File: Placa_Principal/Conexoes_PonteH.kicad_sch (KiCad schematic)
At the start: 6 parts, among them J2 Conn_01x02, J3 Conn_01x02, J4 Conn_01x02, J5 Conn_01x02, U4 L298N MODULE, U5 L298N MODULE

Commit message: Segundo commit
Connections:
- net at U4.2 (IN2L): no longer J3.1 (Pin_1)
- net at U4.1 (IN1L): no longer J3.2 (Pin_2)
- net at U5.1 (IN1L): no longer J5.2 (Pin_2)
- net at U5.2 (IN2L): no longer J5.1 (Pin_1)
- net at U5.3 (IN3L): no longer J4.2 (Pin_2)
- net at U5.4 (IN4L): no longer J4.1 (Pin_1)
- net at U4.3 (IN3L): no longer J2.2 (Pin_2)
- net at U4.4 (IN4L): no longer J2.1 (Pin_1)
- new net ESP_GPIO04: J2.1 (Pin_1)
- new net ESP_GPIO05: J2.2 (Pin_2)
- new net ESP_GPIO06: J3.1 (Pin_1)
- new net ESP_GPIO07: J3.2 (Pin_2)
- new net ESP_GPIO15: J4.1 (Pin_1)
- new net ESP_GPIO16: J4.2 (Pin_2)
- new net ESP_GPIO17: J5.1 (Pin_1)
- new net ESP_GPIO18: J5.2 (Pin_2)
- no-connect marks 14 -> 22
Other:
- moved on the sheet: J2, J3, J4, J5, U4, U5

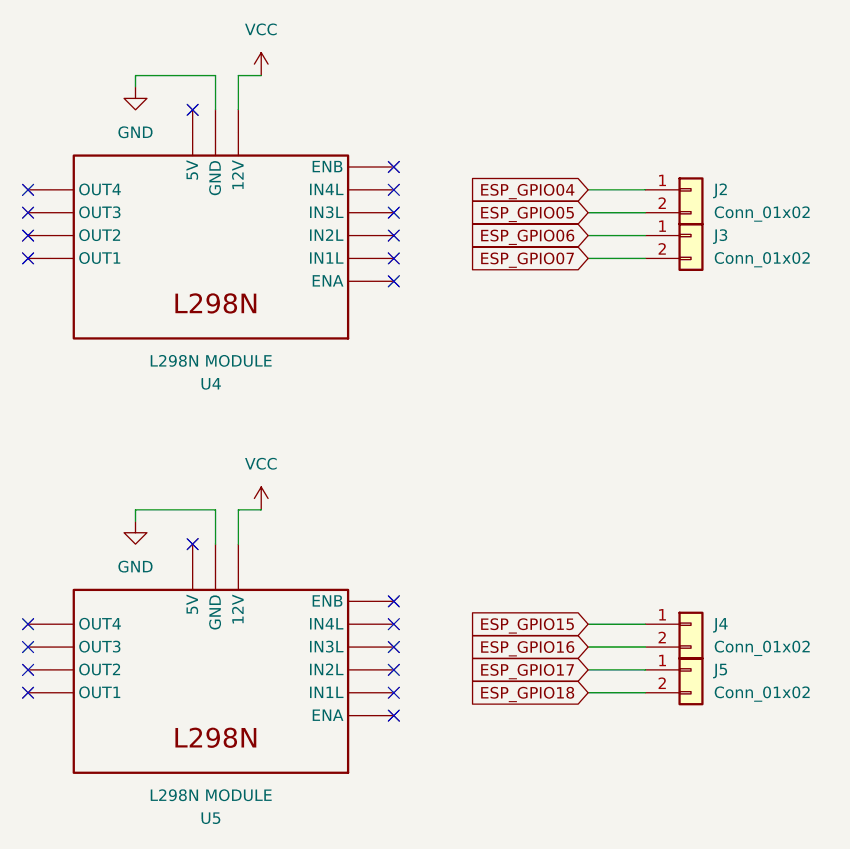
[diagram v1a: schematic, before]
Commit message: Finalizando o esquemático e rearranjando a posição dos componentes na PCB
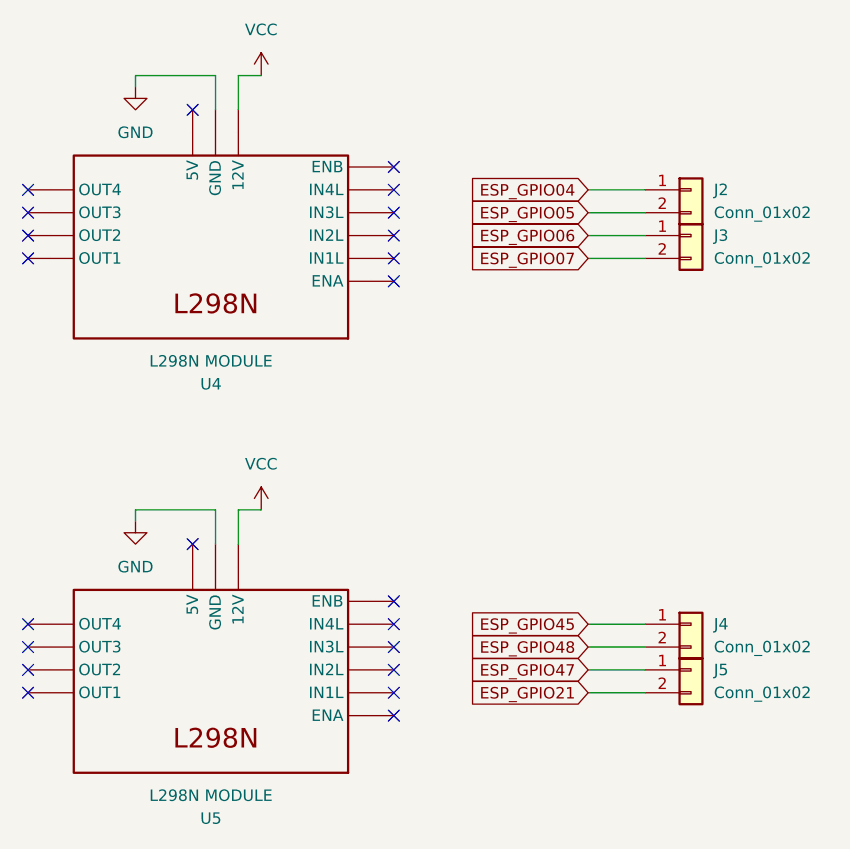
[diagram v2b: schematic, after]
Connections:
- net ESP_GPIO15 renamed ESP_GPIO45
- net ESP_GPIO16 renamed ESP_GPIO48
- net ESP_GPIO17 renamed ESP_GPIO47
- net ESP_GPIO18 renamed ESP_GPIO21
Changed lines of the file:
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@@
 		)
 	)
-	(global_label "ESP_GPIO17"
+	(global_label "ESP_GPIO47"
 		(shape input)
 		(at 185.42 121.92 180)
@@
 		)
 	)
-	(global_label "ESP_GPIO15"
+	(global_label "ESP_GPIO45"
 		(shape input)
 		(at 185.42 116.84 180)
@@
 		)
 	)
-	(global_label "ESP_GPIO16"
+	(global_label "ESP_GPIO48"
 		(shape input)
 		(at 185.42 119.38 180)
@@
 		)
 	)
-	(global_label "ESP_GPIO18"
+	(global_label "ESP_GPIO21"
 		(shape input)
 		(at 185.42 124.46 180)
